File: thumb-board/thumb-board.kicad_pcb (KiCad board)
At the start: 2 copper layers, 53 x 53 mm, 26 parts, among them IC1 TMAG5253BA1IQDMRR, IC10 TMAG5253BA1IQDMRR, IC11 TMAG5253BA1IQDMRR, IC12 TMAG5253BA1IQDMRR, IC2 TMAG5253BA1IQDMRR, IC3 TMAG5253BA1IQDMRR, IC4 TMAG5253BA1IQDMRR, IC5 TMAG5253BA1IQDMRR, IC6 TMAG5253BA1IQDMRR, IC7 TMAG5253BA1IQDMRR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

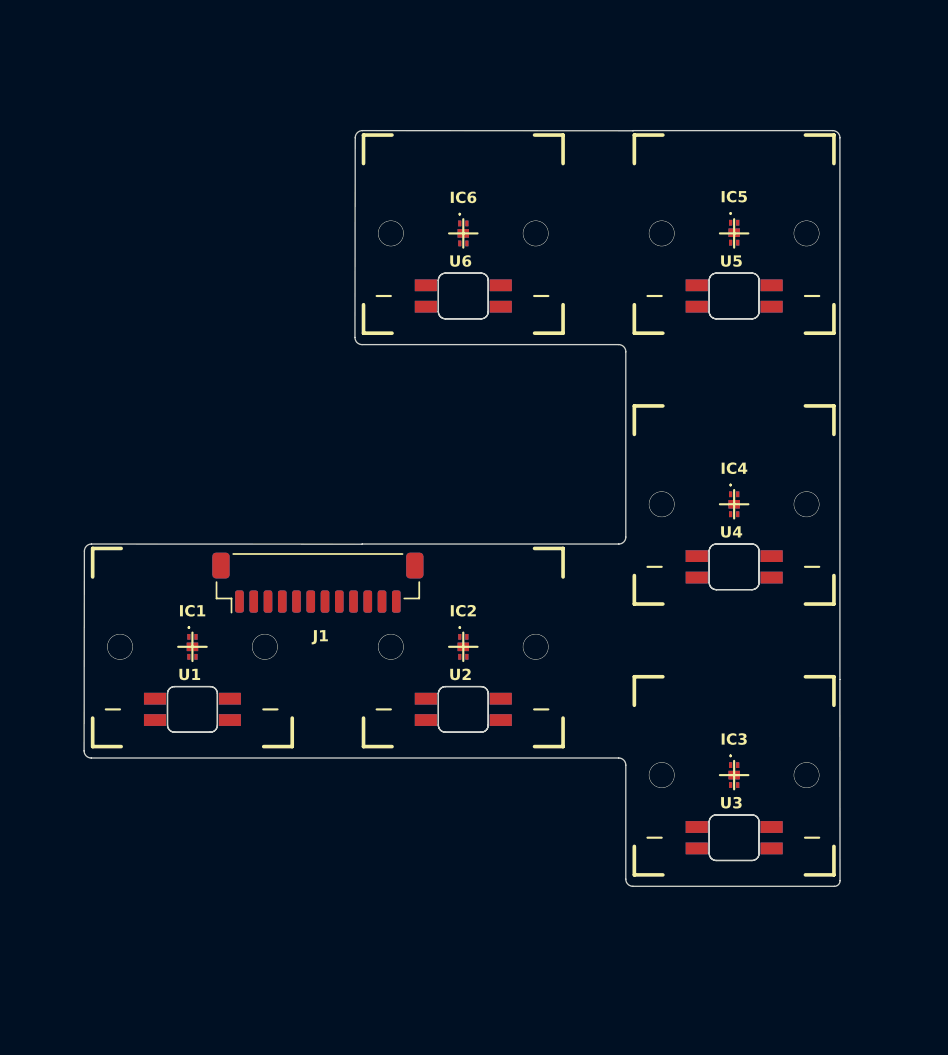
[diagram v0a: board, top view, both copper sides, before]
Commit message: Trace thumb-board
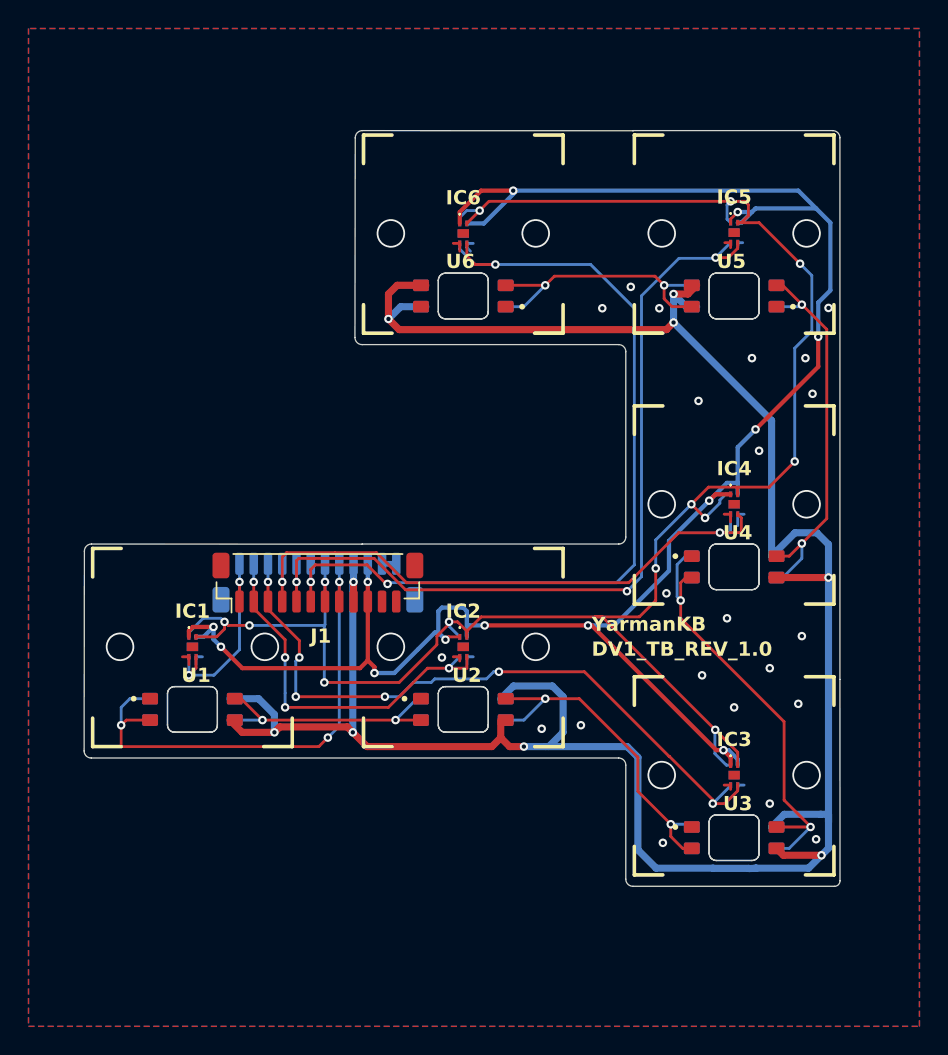
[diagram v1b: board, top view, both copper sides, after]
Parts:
- turned J2 to 0 degrees
- turned U1 to 180 degrees
- turned U11 to 0 degrees
- turned U12 to 0 degrees
- turned U2 to 180 degrees
- turned U3 to 180 degrees
- turned U4 to 180 degrees
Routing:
- net +5V: track 0.00 -> 172.6 mm, vias 0 -> 9
- net +3.3V: track 0.00 -> 142.0 mm, vias 0 -> 13
- net /CMN: track 0.00 -> 136.8 mm, vias 0 -> 13
- net /EN_6: track 0.00 -> 63.0 mm, vias 0 -> 3
- net /EN_5: track 0.00 -> 59.5 mm, vias 0 -> 3
- net /EN_3: track 0.00 -> 48.6 mm, vias 0 -> 6
- net /EN_4: track 0.00 -> 42.5 mm, vias 0 -> 2
- net /DIN: track 0.00 -> 36.6 mm, vias 0 -> 3
- net /D_2: track 0.00 -> 32.5 mm, vias 0 -> 2
- net /D_3: track 0.00 -> 29.3 mm, vias 0 -> 2
- net /EN_2: track 0.00 -> 26.7 mm, vias 0 -> 4
- net /D_1: track 0.00 -> 25.6 mm, vias 0 -> 2
- net /D_4: track 0.00 -> 21.5 mm, vias 0 -> 2
- net /D_0: track 0.00 -> 19.4 mm, vias 0 -> 2
- net /EN_1: track 0.00 -> 14.5 mm, vias 0 -> 2
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- added copper zone on B.Cu, net GND
- added copper zone on F.Cu, net GND
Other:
- board text added: "DV1_TB_REV_1.0"
- board text added: "YarmanKB"
